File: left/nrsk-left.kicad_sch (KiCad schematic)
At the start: 129 parts, among them J1 PJ-320D, J2 USB-C, J3 OLED 128x32, SW1 Esc, SW10 1, SW11 2, SW12 3, SW13 4, SW14 5, SW15 6, SW16 16, SW17 Tab, SW18 Q, SW19 W, SW2 F1, SW20 E, SW21 R, SW22 T, SW23 23, SW24 Ctrl, SW25 A, SW26 S, SW27 D, SW28 F, SW29 G, SW3 F2, SW30 30, SW31 Shift, SW32 Z, SW33 X, SW34 C, SW35 V, SW36 B, SW37 37, SW38 Ctrl, SW39 Opt, SW4 F3, SW40 Cmd, SW41 Space, SW42 Space, SW43 Space, SW44 44, SW5 F4, SW6 F5, SW7 F6, SW8 8, SW9 `, U1 RP2040, U2 USBLC6-2SC6, U4 AP2112K-3.3, U5 W25Q128JVS, Y1 12MHz

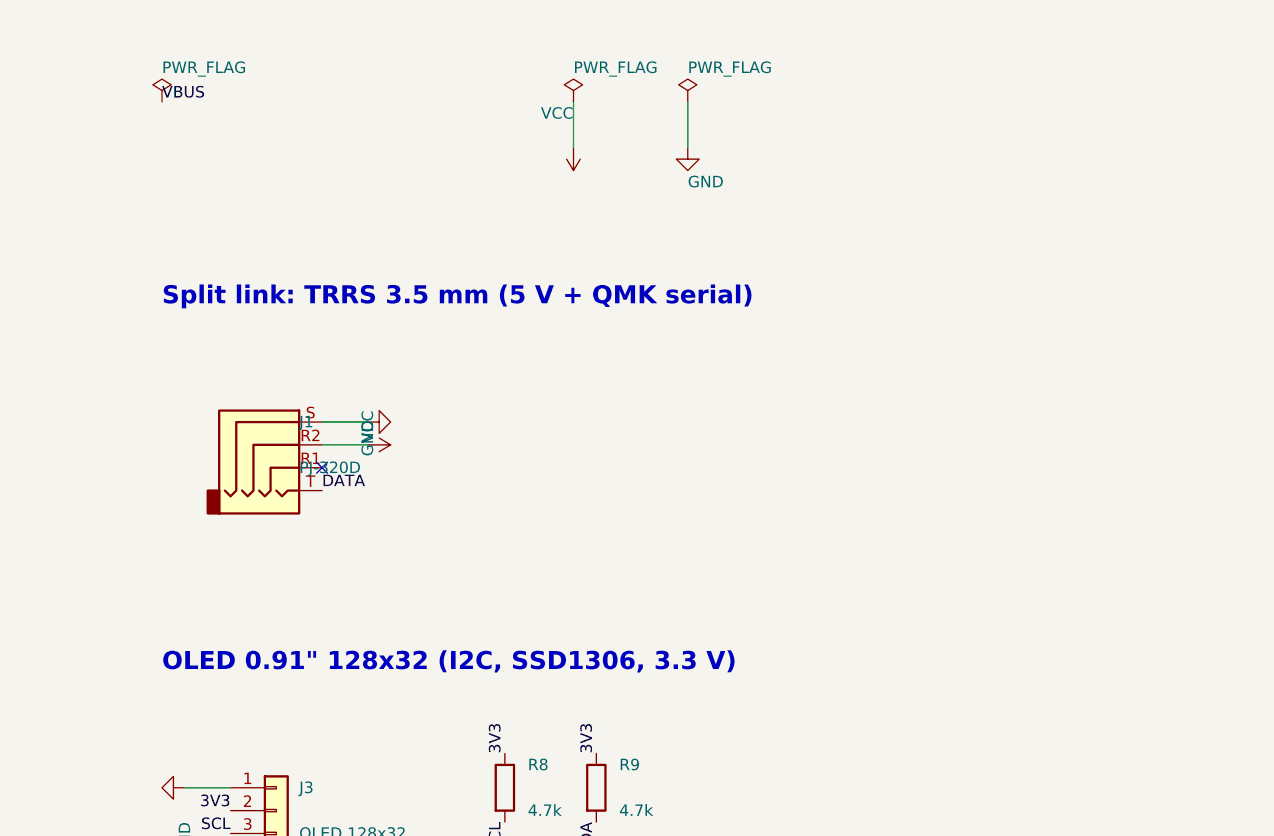
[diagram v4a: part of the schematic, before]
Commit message: Split link over USB-C instead of TRRS, so both port openings line up
The TRRS jack (PJ-320D) hung 5.0 mm under the PCB with its axis 2.5 mm down,
while the USB-C shell's axis is 1.63 mm down, so the two openings in the back
wall sat at different heights. The link now uses a second HRO TYPE-C-31-M-12:
same part, same height, same rounded slot.

- J1 is a USB-C receptacle: VBUS = VCC, D+ (A6/B6) = DATA (GP1), GND; D- and
  CC open, so a host or charger plugged in by mistake keeps VBUS off.
- PCB / case / JLC / BOM generators: the 'trrs' connector kind becomes 'link'
  and is handled like the host USB-C; PJ-320D footprint, model and JLC fix go.
- BOM: 4 USB-C receptacles, a C-C data cable for the link; one fewer
  Extended JLC part (9).
- Docs: README, ordering, pre-order checklist, thumbwheel check, assembly
  guide updated (pinout, which port is which, data cable required).
- Rebuilt: schematics, PCBs (0 unconnected, 0 parity issues, 4 silk warnings
  per side), fab outputs, case, BOM, JLC files, KiCad doc images.

Co-Authored-By: Claude Opus 5.5 <noreply@anthropic.com>
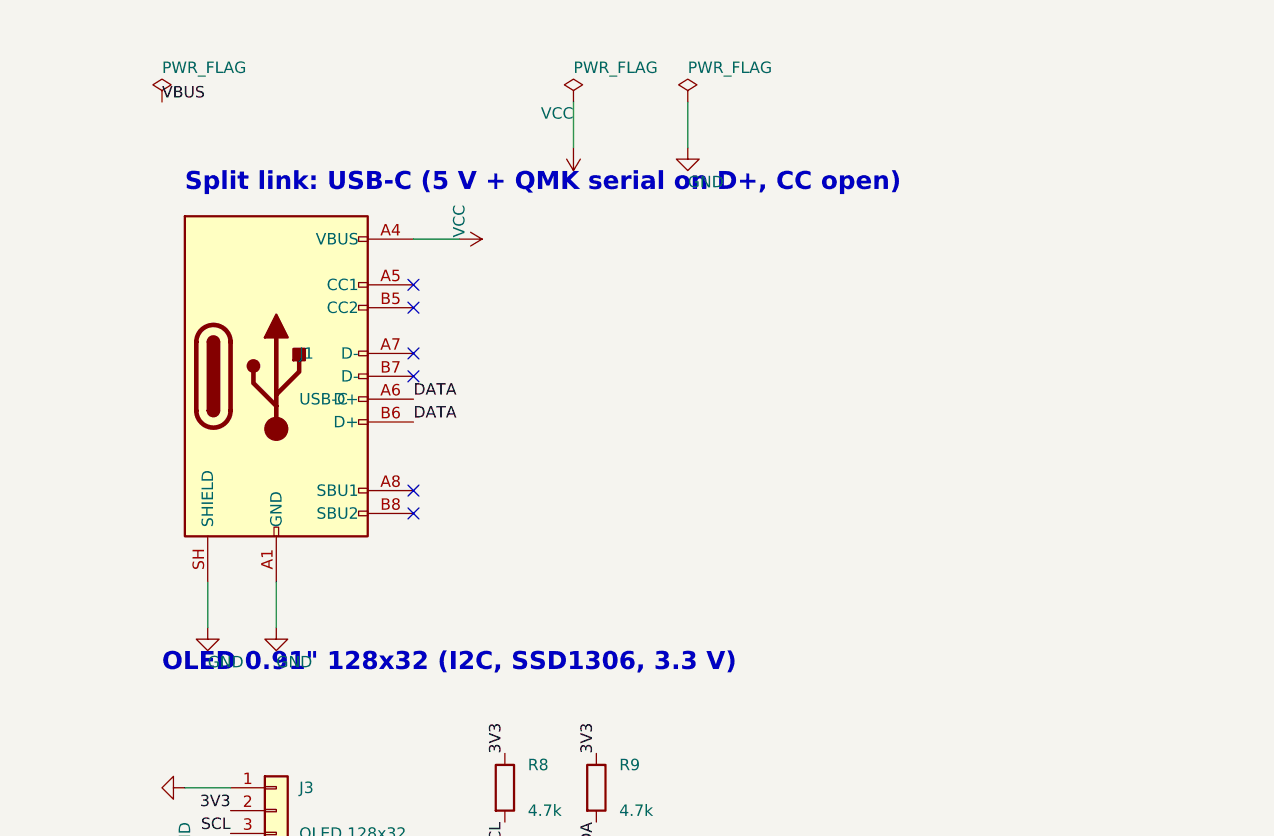
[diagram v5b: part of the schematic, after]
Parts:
- J1: value PJ-320D -> USB-C; footprint Connector_Audio:Jack_3.5mm_PJ320D_Horizontal -> Connector_USB:USB_C_Receptacle_HRO_TYPE-C-31-M-12; symbol Connector_Audio:AudioJack4 -> Connector:USB_C_Receptacle_USB2.0_16P
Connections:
- net DATA: now also J1.A6 (D+), J1.B6 (D+); no longer J1.T
- net GND: now also J1.A1 (GND), J1.A12 (GND), J1.B1 (GND), J1.B12 (GND), J1.SH (SHIELD); no longer J1.S
- net VCC: now also J1.A4 (VBUS), J1.A9 (VBUS), J1.B4 (VBUS), J1.B9 (VBUS); no longer J1.R2
- no-connect marks 16 -> 21
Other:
- note added: "Split link: USB-C (5 V + QMK serial on D+, CC open)"
- note removed: "Split link: TRRS 3.5 mm (5 V + QMK serial)"
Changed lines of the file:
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@@
 	  (instances (project "nrsk-left" (path "/6c78887a-19a2-5291-a4e1-47e49dcf604a" (reference "#PWR039") (unit 1))))
 	)
-	(text "Split link: TRRS 3.5 mm (5 V + QMK serial)" (exclude_from_sim no) (at 330.20 160.02 0) (effects (font (size 2.0 2.0) (bold yes)) (justify left bottom)))
-	(symbol (lib_id "Connector_Audio:AudioJack4") (at 342.90 175.26 0) (unit 1) (exclude_from_sim no) (in_bom yes) (on_board yes) (dnp no)
-	  (property "Reference" "J1" (at 345.44 172.72 0) (effects (font (size 1.27 1.27)) (justify left)))
-	  (property "Value" "PJ-320D" (at 345.44 177.80 0) (effects (font (size 1.27 1.27)) (justify left)))
-	  (property "Footprint" "Connector_Audio:Jack_3.5mm_PJ320D_Horizontal" (at 342.90 175.26 0) (effects (font (size 1.27 1.27)) (hide yes)))
-	  (property "Datasheet" "" (at 342.90 175.26 0) (effects (font (size 1.27 1.27)) (hide yes)))
-	  (pin "R1")
-	  (pin "R2")
-	  (pin "S")
-	  (pin "T")
+	(text "Split link: USB-C (5 V + QMK serial on D+, CC open)" (exclude_from_sim no) (at 332.74 147.32 0) (effects (font (size 2.0 2.0) (bold yes)) (justify left bottom)))
+	(symbol (lib_id "Connector:USB_C_Receptacle_USB2.0_16P") (at 342.90 167.64 0) (unit 1) (exclude_from_sim no) (in_bom yes) (on_board yes) (dnp no)
+	  (property "Reference" "J1" (at 345.44 165.10 0) (effects (font (size 1.27 1.27)) (justify left)))
+	  (property "Value" "USB-C" (at 345.44 170.18 0) (effects (font (size 1.27 1.27)) (justify left)))
+	  (property "Footprint" "Connector_USB:USB_C_Receptacle_HRO_TYPE-C-31-M-12" (at 342.90 167.64 0) (effects (font (size 1.27 1.27)) (hide yes)))
+	  (property "Datasheet" "" (at 342.90 167.64 0) (effects (font (size 1.27 1.27)) (hide yes)))
+	  (pin "A1")
+	  (pin "A4")
+	  (pin "A5")
+	  (pin "A6")
+	  (pin "A7")
+	  (pin "A8")
+	  (pin "A9")
+	  (pin "A12")
+	  (pin "B1")
+	  (pin "B4")
+	  (pin "B5")
+	  (pin "B6")
+	  (pin "B7")
+	  (pin "B8")
+	  (pin "B9")
+	  (pin "B12")
+	  (pin "SH")
 	  (instances (project "nrsk-left" (path "/6c78887a-19a2-5291-a4e1-47e49dcf604a" (reference "J1") (unit 1))))
 	)
-	(no_connect (at 347.98 177.80))
-	(wire (pts (xy 347.98 175.26) (xy 353.06 175.26)) (stroke (width 0) (type default)))
-	(symbol (lib_id "power:VCC") (at 353.06 175.26 270) (unit 1) (exclude_from_sim no) (in_bom no) (on_board no) (dnp no)
-	  (property "Reference" "#PWR040" (at 353.06 175.26 0) (effects (font (size 1.27 1.27)) (justify left) (hide yes)))
-	  (property "Value" "VCC" (at 353.06 171.45 0) (effects (font (size 1.27 1.27)) (justify left)))
-	  (property "Footprint" "" (at 353.06 175.26 0) (effects (font (size 1.27 1.27)) (hide yes)))
-	  (property "Datasheet" "" (at 353.06 175.26 0) (effects (font (size 1.27 1.27)) (hide yes)))
+	(wire (pts (xy 342.90 190.50) (xy 342.90 195.58)) (stroke (width 0) (type default)))
+	(symbol (lib_id "power:GND") (at 342.90 195.58 0) (unit 1) (exclude_from_sim no) (in_bom no) (on_board no) (dnp no)
+	  (property "Reference" "#PWR040" (at 342.90 195.58 0) (effects (font (size 1.27 1.27)) (justify left) (hide yes)))
+	  (property "Value" "GND" (at 342.90 199.39 0) (effects (font (size 1.27 1.27)) (justify left)))
+	  (property "Footprint" "" (at 342.90 195.58 0) (effects (font (size 1.27 1.27)) (hide yes)))
+	  (property "Datasheet" "" (at 342.90 195.58 0) (effects (font (size 1.27 1.27)) (hide yes)))
 	  (pin "1")
 	  (instances (project "nrsk-left" (path "/6c78887a-19a2-5291-a4e1-47e49dcf604a" (reference "#PWR040") (unit 1))))
 	)
-	(wire (pts (xy 347.98 172.72) (xy 353.06 172.72)) (stroke (width 0) (type default)))
-	(symbol (lib_id "power:GND") (at 353.06 172.72 90) (unit 1) (exclude_from_sim no) (in_bom no) (on_board no) (dnp no)
-	  (property "Reference" "#PWR041" (at 353.06 172.72 0) (effects (font (size 1.27 1.27)) (justify left) (hide yes)))
-	  (property "Value" "GND" (at 353.06 176.53 0) (effects (font (size 1.27 1.27)) (justify left)))
-	  (property "Footprint" "" (at 353.06 172.72 0) (effects (font (size 1.27 1.27)) (hide yes)))
-	  (property "Datasheet" "" (at 353.06 172.72 0) (effects (font (size 1.27 1.27)) (hide yes)))
+	(wire (pts (xy 358.14 152.40) (xy 363.22 152.40)) (stroke (width 0) (type default)))
+	(symbol (lib_id "power:VCC") (at 363.22 152.40 270) (unit 1) (exclude_from_sim no) (in_bom no) (on_board no) (dnp no)
+	  (property "Reference" "#PWR041" (at 363.22 152.40 0) (effects (font (size 1.27 1.27)) (justify left) (hide yes)))
+	  (property "Value" "VCC" (at 363.22 148.59 0) (effects (font (size 1.27 1.27)) (justify left)))
+	  (property "Footprint" "" (at 363.22 152.40 0) (effects (font (size 1.27 1.27)) (hide yes)))
+	  (property "Datasheet" "" (at 363.22 152.40 0) (effects (font (size 1.27 1.27)) (hide yes)))
 	  (pin "1")
 	  (instances (project "nrsk-left" (path "/6c78887a-19a2-5291-a4e1-47e49dcf604a" (reference "#PWR041") (unit 1))))
 	)
-	(label "DATA" (at 347.98 180.34 0) (effects (font (size 1.27 1.27)) (justify left bottom)))
+	(no_connect (at 358.14 157.48))
+	(label "DATA" (at 358.14 170.18 0) (effects (font (size 1.27 1.27)) (justify left bottom)))
+	(no_connect (at 358.14 165.10))
+	(no_connect (at 358.14 180.34))
+	(no_connect (at 358.14 160.02))
+	(label "DATA" (at 358.14 172.72 0) (effects (font (size 1.27 1.27)) (justify left bottom)))
+	(no_connect (at 358.14 167.64))
+	(no_connect (at 358.14 182.88))
+	(wire (pts (xy 335.28 190.50) (xy 335.28 195.58)) (stroke (width 0) (type default)))
+	(symbol (lib_id "power:GND") (at 335.28 195.58 0) (unit 1) (exclude_from_sim no) (in_bom no) (on_board no) (dnp no)
+	  (property "Reference" "#PWR042" (at 335.28 195.58 0) (effects (font (size 1.27 1.27)) (justify left) (hide yes)))
+	  (property "Value" "GND" (at 335.28 199.39 0) (effects (font (size 1.27 1.27)) (justify left)))
+	  (property "Footprint" "" (at 335.28 195.58 0) (effects (font (size 1.27 1.27)) (hide yes)))
+	  (property "Datasheet" "" (at 335.28 195.58 0) (effects (font (size 1.27 1.27)) (hide yes)))
+	  (pin "1")
+	  (instances (project "nrsk-left" (path "/6c78887a-19a2-5291-a4e1-47e49dcf604a" (reference "#PWR042") (unit 1))))
+	)
 	(text "OLED 0.91\" 128x32 (I2C, SSD1306, 3.3 V)" (exclude_from_sim no) (at 330.20 200.66 0) (effects (font (size 2.0 2.0) (bold yes)) (justify left bottom)))
 	(symbol (lib_id "Connector_Generic:Conn_01x04") (at 342.90 215.90 0) (unit 1) (exclude_from_sim no) (in_bom yes) (on_board yes) (dnp no)
@@
 	(wire (pts (xy 337.82 213.36) (xy 332.74 213.36)) (stroke (width 0) (type default)))
 	(symbol (lib_id "power:GND") (at 332.74 213.36 270) (unit 1) (exclude_from_sim no) (in_bom no) (on_board no) (dnp no)
-	  (property "Reference" "#PWR042" (at 332.74 213.36 0) (effects (font (size 1.27 1.27)) (justify left) (hide yes)))
+	  (property "Reference" "#PWR043" (at 332.74 213.36 0) (effects (font (size 1.27 1.27)) (justify left) (hide yes)))
 	  (property "Value" "GND" (at 332.74 217.17 0) (effects (font (size 1.27 1.27)) (justify left)))
 	  (property "Footprint" "" (at 332.74 213.36 0) (effects (font (size 1.27 1.27)) (hide yes)))
 	  (property "Datasheet" "" (at 332.74 213.36 0) (effects (font (size 1.27 1.27)) (hide yes)))
 	  (pin "1")
-	  (instances (project "nrsk-left" (path "/6c78887a-19a2-5291-a4e1-47e49dcf604a" (reference "#PWR042") (unit 1))))
+	  (instances (project "nrsk-left" (path "/6c78887a-19a2-5291-a4e1-47e49dcf604a" (reference "#PWR043") (unit 1))))
 	)
 	(label "3V3" (at 337.82 215.90 180) (effects (font (size 1.27 1.27)) (justify right bottom)))
@@
 	(wire (pts (xy 335.28 254.00) (xy 330.20 254.00)) (stroke (width 0) (type default)))
 	(symbol (lib_id "power:GND") (at 330.20 254.00 270) (unit 1) (exclude_from_sim no) (in_bom no) (on_board no) (dnp no)
-	  (property "Reference" "#PWR043" (at 330.20 254.00 0) (effects (font (size 1.27 1.27)) (justify left) (hide yes)))
+	  (property "Reference" "#PWR044" (at 330.20 254.00 0) (effects (font (size 1.27 1.27)) (justify left) (hide yes)))
 	  (property "Value" "GND" (at 330.20 257.81 0) (effects (font (size 1.27 1.27)) (justify left)))
 	  (property "Footprint" "" (at 330.20 254.00 0) (effects (font (size 1.27 1.27)) (hide yes)))
 	  (property "Datasheet" "" (at 330.20 254.00 0) (effects (font (size 1.27 1.27)) (hide yes)))
 	  (pin "1")
-	  (instances (project "nrsk-left" (path "/6c78887a-19a2-5291-a4e1-47e49dcf604a" (reference "#PWR043") (unit 1))))
+	  (instances (project "nrsk-left" (path "/6c78887a-19a2-5291-a4e1-47e49dcf604a" (reference "#PWR044") (unit 1))))
 	)
 	(sheet_instances (path "/" (page "1")))

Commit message: Remove the blank inner key column on both halves; even plate band round the OLED cover
KLE: the unlabeled keys of the inner column go (left 8, 16, 23, 30, 37, 44; right 71, 73, 75, 77, 79, 81), so
the halves have 38 + 42 = 80 keys. The right "\" key now sits in its own row (row 2, col 7) and the remap goes;
the left's COL7 stays unconnected in the schematic.

The gap is closed: the right board moves its keys one unit in (key_shift +1 u, width -1 u). The left board is
sized from its row 0-1 keycaps: COVER_FRAME + the OLED cover (window + 5 mm each side) + COVER_FRAME, less the
case wall, so it narrows by 15.4 mm instead of a full unit.

The OLED's half-mirror cover is now laid out from the plate band round it: 3.5 mm to the case outline (top and
inner edge), to the nearest row 0-1 keycaps, and to the row-2 keycap line below, on both halves; the corner at the
case corner is concentric with it (R9), the others R2. The OLED stays at its height: its display glass, 3 mm
toward the module's top, lands at the cover's centre, and higher up the module would leave the board's rounded
corner and meet the link USB-C's shield pins. make_case checks the band against keycaps and the outline.

Sizes: boards 157.1 / 180.5 x 126.3 mm, cases 174.1 / 197.5 x 143.3 mm. The drum stays centred on Backspace.
Docs (README, ordering, pre-order checklist, drum spec coordinates) follow: 80 switches / sockets / diodes,
69 1 u keycaps, LCSC 85 switches and 90 sockets, trays fit a 220 mm bed.

Checked: ./build.sh -> left 0 unconnected (31 zero-length router stubs removed), right 0 unconnected, 0 parity
issues, ERC 0 / 0; DRC 4 silkscreen-at-board-edge warnings per side, as on main; make_case.py checks ok on both
halves (OLED band, drum dial); make_jlc: left 77, right 81 placements; textlint 0 on the edited docs.

Co-Authored-By: Claude Opus 5.5 <noreply@anthropic.com>
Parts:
- removed D39, D40, D41, D42, D43, D44: 1N4148W, Diode_SMD:D_SOD-123, symbol Device:D
- removed SW39: Opt, nrsk:SW_MX_Hotswap_1.25u, symbol Switch:SW_Push
- removed SW40: Cmd, nrsk:SW_MX_Hotswap_1.25u, symbol Switch:SW_Push
- removed SW41, SW42, SW43: Space, nrsk:SW_MX_Hotswap_1.00u, symbol Switch:SW_Push
- removed SW44: 44, nrsk:SW_MX_Hotswap_1.00u, symbol Switch:SW_Push
- SW10: value 1 -> 2
- SW11: value 2 -> 3
- SW12: value 3 -> 4
- SW13: value 4 -> 5
- SW14: value 5 -> 6
- SW15: value 6 -> Tab; footprint nrsk:SW_MX_Hotswap_1.00u -> nrsk:SW_MX_Hotswap_1.50u
- SW16: value 16 -> Q
- SW17: value Tab -> W; footprint nrsk:SW_MX_Hotswap_1.50u -> nrsk:SW_MX_Hotswap_1.00u
- SW18: value Q -> E
- SW19: value W -> R
- SW20: value E -> T
- SW21: value R -> Ctrl; footprint nrsk:SW_MX_Hotswap_1.00u -> nrsk:SW_MX_Hotswap_1.75u
- SW22: value T -> A
- SW23: value 23 -> S
- SW24: value Ctrl -> D; footprint nrsk:SW_MX_Hotswap_1.75u -> nrsk:SW_MX_Hotswap_1.00u
- SW25: value A -> F
- SW26: value S -> G
- SW27: value D -> Shift; footprint nrsk:SW_MX_Hotswap_1.00u -> nrsk:SW_MX_Hotswap_2.25u
- SW28: value F -> Z
- SW29: value G -> X
- SW30: value 30 -> C
- SW31: value Shift -> V; footprint nrsk:SW_MX_Hotswap_2.25u -> nrsk:SW_MX_Hotswap_1.00u
- SW32: value Z -> B
- SW33: value X -> Ctrl; footprint nrsk:SW_MX_Hotswap_1.00u -> nrsk:SW_MX_Hotswap_1.25u
- SW34: value C -> Opt; footprint nrsk:SW_MX_Hotswap_1.00u -> nrsk:SW_MX_Hotswap_1.25u
- SW35: value V -> Cmd; footprint nrsk:SW_MX_Hotswap_1.00u -> nrsk:SW_MX_Hotswap_1.25u
- SW36: value B -> Space
- SW37: value 37 -> Space
- SW38: value Ctrl -> Space; footprint nrsk:SW_MX_Hotswap_1.25u -> nrsk:SW_MX_Hotswap_1.00u
- SW8: value 8 -> `
- SW9: value ` -> 1
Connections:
- net COL0: now also SW15.1, SW21.1, SW27.1, SW33.1, SW8.1; no longer SW17.1, SW24.1, SW31.1, SW38.1, SW9.1
- net COL1: now also SW16.1, SW22.1, SW28.1, SW34.1, SW9.1; no longer SW10.1, SW18.1, SW25.1, SW32.1
- net COL2: now also SW10.1, SW17.1, SW23.1, SW29.1, SW35.1; no longer SW11.1, SW19.1, SW26.1, SW33.1
- net COL3: now also SW11.1, SW18.1, SW24.1, SW30.1, SW36.1; no longer SW12.1, SW20.1, SW27.1, SW34.1
- net COL4: now also SW12.1, SW19.1, SW25.1, SW31.1, SW37.1; no longer SW13.1, SW21.1, SW28.1, SW35.1
- net COL5: now also SW13.1, SW20.1, SW26.1, SW32.1, SW38.1; no longer SW14.1, SW22.1, SW29.1, SW36.1
- net COL6: now also SW14.1; no longer SW15.1, SW23.1, SW30.1, SW37.1
- net ROW0: no longer D8.1 (K)
- net ROW1: now also D8.1 (K); no longer D15.1 (K), D16.1 (K)
- net ROW2: now also D15.1 (K), D16.1 (K); no longer D21.1 (K), D22.1 (K), D23.1 (K)
- net ROW3: now also D21.1 (K), D22.1 (K), D23.1 (K); no longer D27.1 (K), D28.1 (K), D29.1 (K), D30.1 (K)
- net ROW4: now also D27.1 (K), D28.1 (K), D29.1 (K), D30.1 (K); no longer D33.1 (K), D34.1 (K), D35.1 (K), D36.1 (K), D37.1 (K)
- net ROW5: now also D33.1 (K), D34.1 (K), D35.1 (K), D36.1 (K), D37.1 (K)
- removed net COL7: SW16.1, SW8.1, U1.29 (GPIO18)
- no-connect marks 21 -> 22
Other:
- note added: "Key matrix (left half, COL2ROW, 38 keys)"
- note removed: "COL7"
- note removed: "Key matrix (left half, COL2ROW, 44 keys)"
- moved on the sheet: D10, D11, D12, D13, D14, D15, D16, D17, D18, D19, D20, D21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

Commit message: Move the RP2040 and its support parts to the front, visible through the clear plate
- RP2040, flash, crystal, LDO, decoupling caps and resistors on the front, in the
  key-free strip along the inner edge (clear of every keycap and the OLED cover);
  USB-C and its protection parts, reset switch and BOOTSEL pad stay on the back
- RP2040 fixed with pin 1 top-left so its Raspberry Pi logo reads upright
  (datasheet Figure 168); make_pcb asserts the orientation
- Left half: pin row 1-14 faces the keys, so it is fanned out to 1 mm pitch and
  the matrix rows are routed by make_pcb; Freerouting does the rest
- build.sh retries routing until 0 unconnected and 0 DRC violations
- USB-C footprint copy in lib/nrsk.pretty with its outline on Fab (no clipped silk)
- JLC CPL handles top-side parts; front assembly drawing added
- Printed plate B: web cut away over the front-side parts
- DRC (all severities) 0, unconnected 0, parity 0, ERC 0 on both halves
- Docs, renders, fab outputs and case files regenerated

Co-Authored-By: Claude Opus 5.5 <noreply@anthropic.com>
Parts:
- J1, J2: footprint Connector_USB:USB_C_Receptacle_HRO_TYPE-C-31-M-12 -> nrsk:USB_C_Receptacle_HRO_TYPE-C-31-M-12
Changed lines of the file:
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@@
 	  (property "Reference" "J2" (at 345.44 58.42 0) (effects (font (size 1.27 1.27)) (justify left)))
 	  (property "Value" "USB-C" (at 345.44 63.50 0) (effects (font (size 1.27 1.27)) (justify left)))
-	  (property "Footprint" "Connector_USB:USB_C_Receptacle_HRO_TYPE-C-31-M-12" (at 342.90 60.96 0) (effects (font (size 1.27 1.27)) (hide yes)))
+	  (property "Footprint" "nrsk:USB_C_Receptacle_HRO_TYPE-C-31-M-12" (at 342.90 60.96 0) (effects (font (size 1.27 1.27)) (hide yes)))
 	  (property "Datasheet" "" (at 342.90 60.96 0) (effects (font (size 1.27 1.27)) (hide yes)))
 	  (pin "A1")
@@
 	  (property "Reference" "J1" (at 345.44 165.10 0) (effects (font (size 1.27 1.27)) (justify left)))
 	  (property "Value" "USB-C" (at 345.44 170.18 0) (effects (font (size 1.27 1.27)) (justify left)))
-	  (property "Footprint" "Connector_USB:USB_C_Receptacle_HRO_TYPE-C-31-M-12" (at 342.90 167.64 0) (effects (font (size 1.27 1.27)) (hide yes)))
+	  (property "Footprint" "nrsk:USB_C_Receptacle_HRO_TYPE-C-31-M-12" (at 342.90 167.64 0) (effects (font (size 1.27 1.27)) (hide yes)))
 	  (property "Datasheet" "" (at 342.90 167.64 0) (effects (font (size 1.27 1.27)) (hide yes)))
 	  (pin "A1")
